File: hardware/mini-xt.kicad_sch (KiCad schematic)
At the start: 0 parts

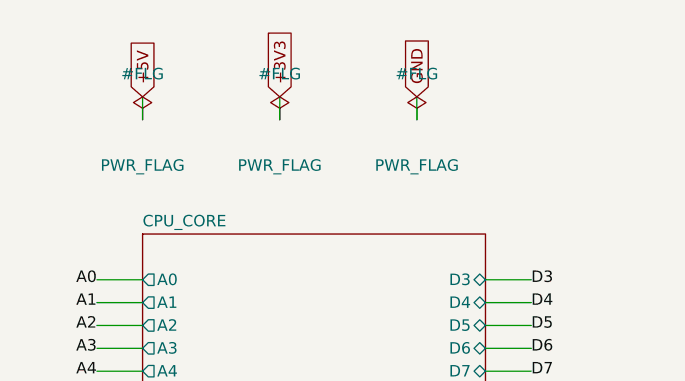
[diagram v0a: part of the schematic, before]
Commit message: ERC power cleanup: single flag owner, flags on series-fed rails
Full-build ERC is now just the 6 expected IRQ9-13/15 label_dangling.

- Root's duplicate PWR_FLAGs removed from build.py: power.py #FLG1-3
  own +5V/+3V3/GND; the pair made flag-vs-flag pin_to_pin errors.
- PWR_FLAGs added on the local rails ERC can't see through a series
  part: VBUS_MCU / VBUS_VID (Schottky diode-OR), VBUS_KBD / HDMI_5V
  (polyfuse), CH224_VDD (1k per WCH ref), AVDD_PGUS / AGND_PGUS
  (ferrite beads).

Net membership verified unchanged: 821 nets, node-identical to HEAD.

Co-Authored-By: Claude Fable 5 <noreply@anthropic.com>
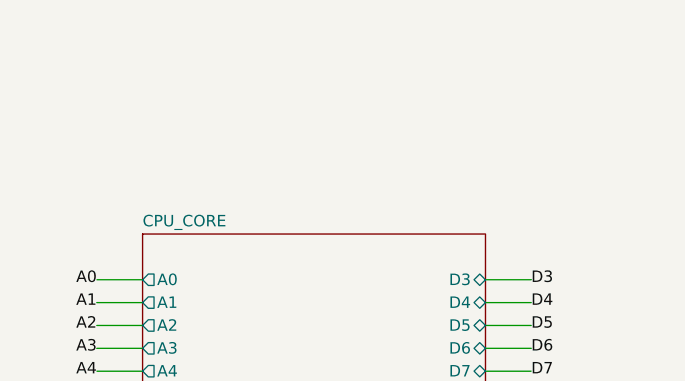
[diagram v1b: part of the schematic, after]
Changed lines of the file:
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@@
-		)
-	)
-	(wire
-		(pts
-			(xy 25.4 12.7)
-			(xy 25.4 10.16)
-		)
-		(stroke
-			(width 0)
-			(type default)
-		)
-	)
-	(global_label "+5V"
-		(shape input)
-		(at 25.4 10.16 90)
-		(effects
-			(font
-				(size 1.27 1.27)
-			)
-		)
-	)
-	(wire
-		(pts
-			(xy 40.64 12.7)
-			(xy 40.64 10.16)
-		)
-		(stroke
-			(width 0)
-			(type default)
-		)
-	)
-	(global_label "+3V3"
-		(shape input)
-		(at 40.64 10.16 90)
-		(effects
-			(font
-				(size 1.27 1.27)
-			)
-		)
-	)
-	(wire
-		(pts
-			(xy 55.88 12.7)
-			(xy 55.88 10.16)
-		)
-		(stroke
-			(width 0)
-			(type default)
-		)
-	)
-	(global_label "GND"
-		(shape input)
-		(at 55.88 10.16 90)
-		(effects
-			(font
-				(size 1.27 1.27)
-			)
-		)
-	)
-	(symbol
-		(lib_id "power:PWR_FLAG")
-		(at 25.4 12.7 0)
-		(unit 1)
-		(exclude_from_sim no)
-		(in_bom yes)
-		(on_board yes)
-		(dnp no)
-		(fields_autoplaced yes)
-		(property "Reference" "#FLG"
-			(at 25.4 7.62 0)
-			(effects
-				(font
-					(size 1.27 1.27)
-				)
-			)
-		)
-		(property "Value" "PWR_FLAG"
-			(at 25.4 17.78 0)
-			(effects
-				(font
-					(size 1.27 1.27)
-				)
-			)
-		)
-		(property "Footprint" ""
-			(at 25.4 12.7 0)
-			(effects
-				(font
-					(size 1.27 1.27)
-				)
-				(hide yes)
-			)
-		)
-		(pin "1"
-		)
-		(instances
-			(project "mini-xt"
-				(path "/26736c46-8b40-5460-874f-03596d17270c"
-					(reference "#FLG")
-					(unit 1)
-				)
-			)
-		)
-	)
-	(symbol
-		(lib_id "power:PWR_FLAG")
-		(at 40.64 12.7 0)
-		(unit 1)
-		(exclude_from_sim no)
-		(in_bom yes)
-		(on_board yes)
-		(dnp no)
-		(fields_autoplaced yes)
-		(property "Reference" "#FLG"
-			(at 40.64 7.62 0)
-			(effects
-				(font
-					(size 1.27 1.27)
-				)
-			)
-		)
-		(property "Value" "PWR_FLAG"
-			(at 40.64 17.78 0)
-			(effects
-				(font
-					(size 1.27 1.27)
-				)
-			)
-		)
-		(property "Footprint" ""
-			(at 40.64 12.7 0)
-			(effects
-				(font
-					(size 1.27 1.27)
-				)
-				(hide yes)
-			)
-		)
-		(pin "1"
-		)
-		(instances
-			(project "mini-xt"
-				(path "/26736c46-8b40-5460-874f-03596d17270c"
-					(reference "#FLG")
-					(unit 1)
-				)
-			)
-		)
-	)
-	(symbol
-		(lib_id "power:PWR_FLAG")
-		(at 55.88 12.7 0)
-		(unit 1)
-		(exclude_from_sim no)
-		(in_bom yes)
-		(on_board yes)
-		(dnp no)
-		(fields_autoplaced yes)
-		(property "Reference" "#FLG"
-			(at 55.88 7.62 0)
-			(effects
-				(font
-					(size 1.27 1.27)
-				)
-			)
-		)
-		(property "Value" "PWR_FLAG"
-			(at 55.88 17.78 0)
-			(effects
-				(font
-					(size 1.27 1.27)
-				)
-			)
-		)
-		(property "Footprint" ""
-			(at 55.88 12.7 0)
-			(effects
-				(font
-					(size 1.27 1.27)
-				)
-				(hide yes)
-			)
-		)
-		(pin "1"
-		)
-		(instances
-			(project "mini-xt"
-				(path "/26736c46-8b40-5460-874f-03596d17270c"
-					(reference "#FLG")
-					(unit 1)
-				)
-			)
 		)
 	)

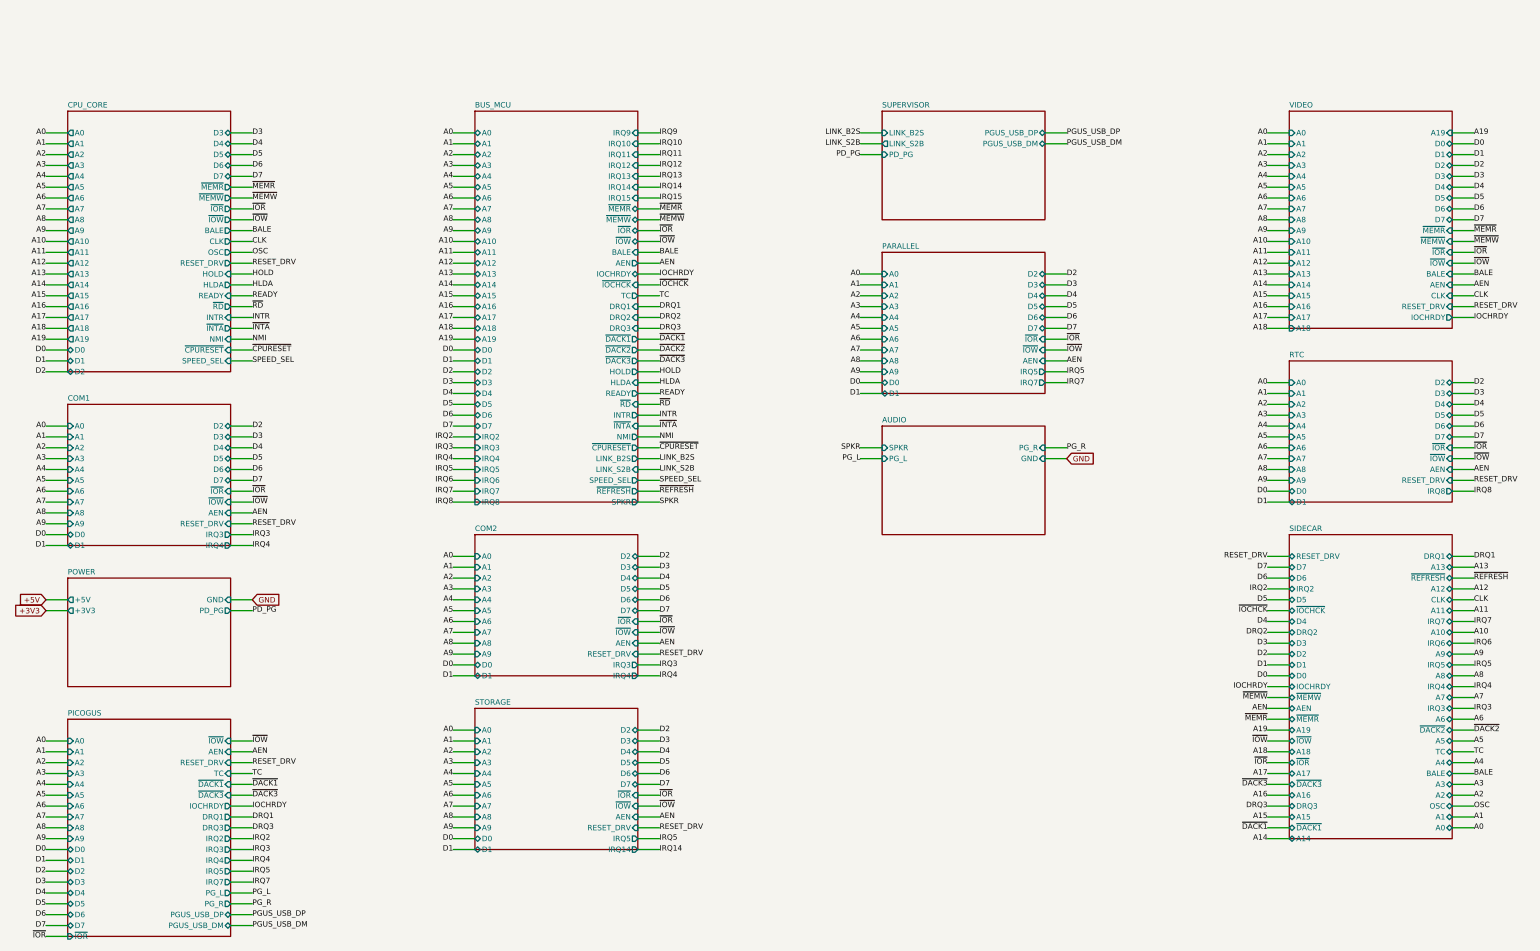
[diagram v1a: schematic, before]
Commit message: IRQ rework: single-'165 collector, hardwired COM/LPT IRQs
- IRQ collector shrunk to one 74HCT165: D0-D6 = IRQ2-8, D7 = IRQ14
  (replacing the source-less IRQ9). U19 + pull-downs R19-R24 + C18
  deleted; IRQ9-13/15 dropped everywhere (nothing on the board or the
  8-bit header can drive them). Firmware shifts 8 bits, Q7-first.
- COM/LPT IRQ straps deleted, hardwired to the PC conventions:
  COM1=IRQ4, COM2=IRQ3 (COM_IRQ per-instance netmap remap -- first use
  of the INSTANCES netmap), LPT=IRQ7 (U13 '125 drives the net
  directly). The enable jumpers (COM JP3, LPT JP2) free an IRQ by
  disabling the port; the tri-state drivers go silent with it.
- Storage JP3 (IRQ14/IRQ5) kept: both positions are real conventions
  (AT vs XT), not conflict avoidance. Its IRQ5 warning now points at
  the PicoGUS jumper block, the only remaining IRQ5 contention.
- Design doc: fix stale claim that IRQ8 rides a reclaimed header pin
  (that pin is a ground return; IRQ8 is motherboard-internal).

Full-build ERC: 0 violations.

Co-Authored-By: Claude Fable 5 <noreply@anthropic.com>
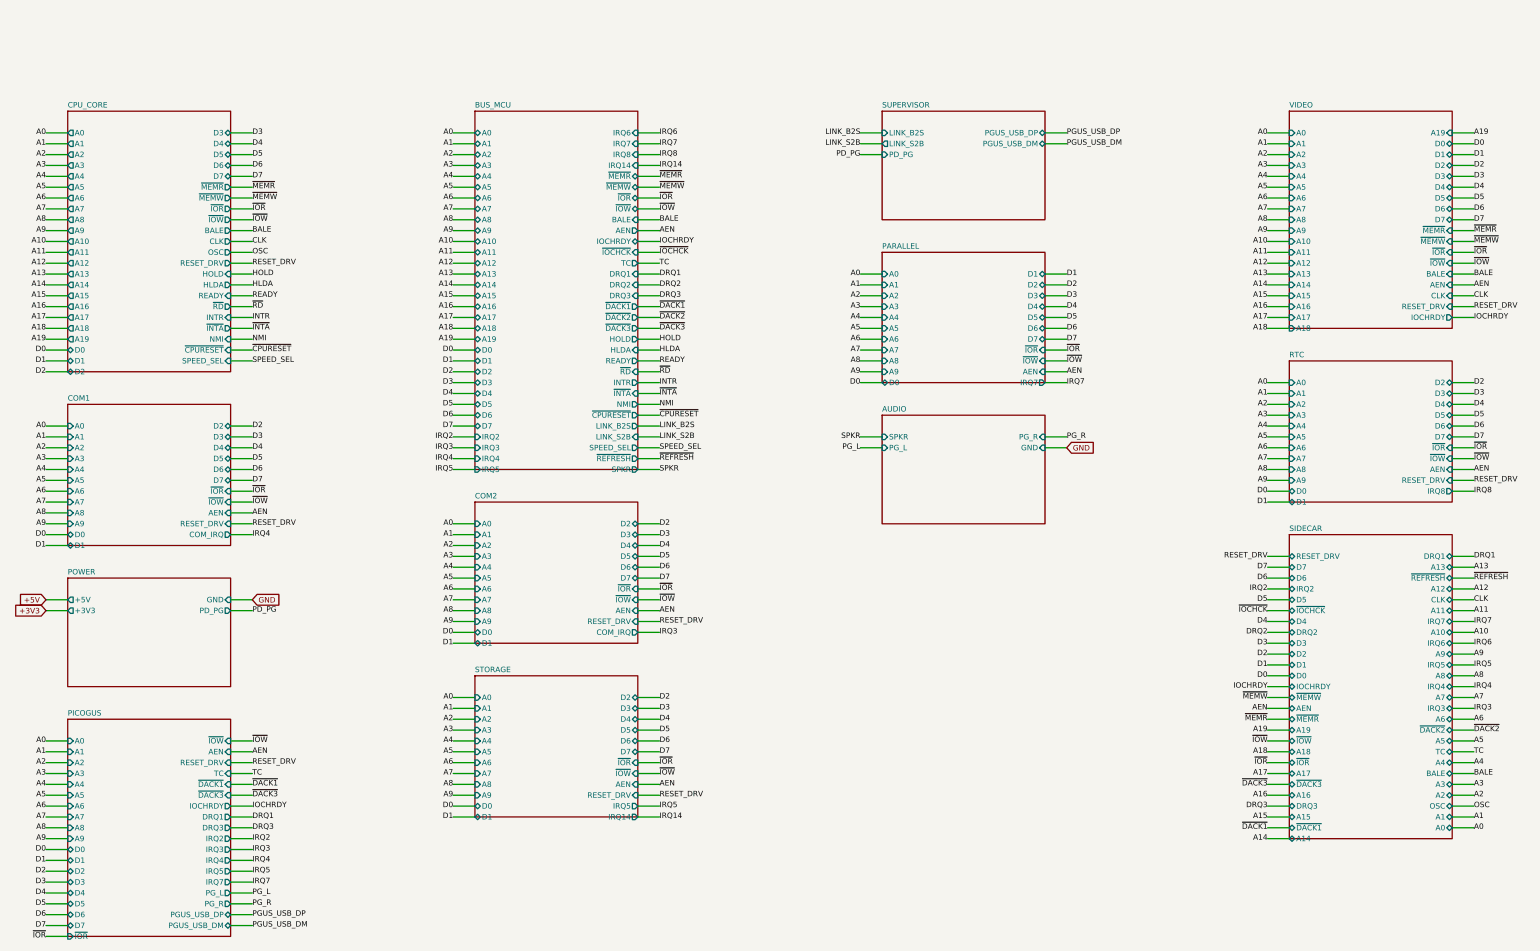
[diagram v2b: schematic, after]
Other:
- sheet BUS_MCU ports: added none; removed IRQ10, IRQ11, IRQ12, IRQ13, IRQ15, IRQ9
- sheet COM1 ports: added COM_IRQ; removed IRQ3, IRQ4
- sheet COM2 ports: added COM_IRQ; removed IRQ3, IRQ4
- sheet PARALLEL ports: added none; removed IRQ5

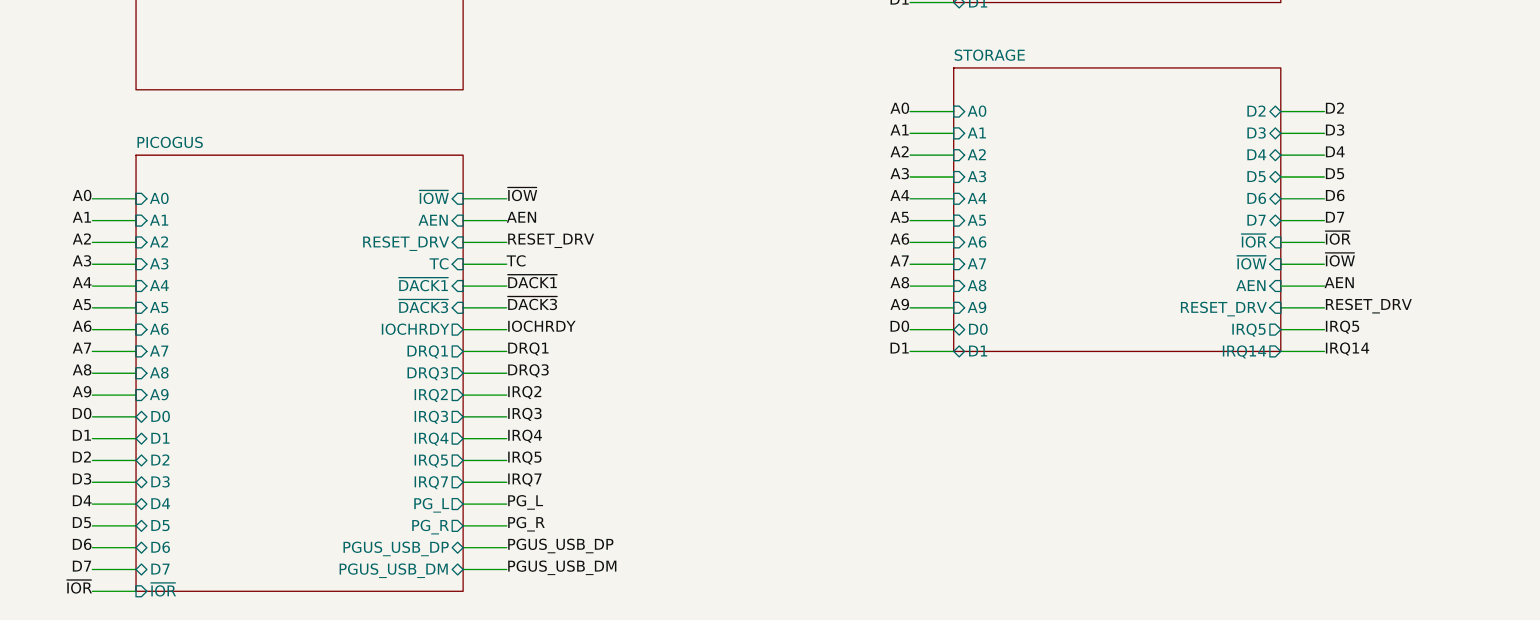
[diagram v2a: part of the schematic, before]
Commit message: Hardwire storage IRQ14 and PicoGUS IRQ5; drop their IRQ jumpers
- Storage JP3 deleted: INTRQ -> '125 -> IRQ14 directly (the soft PIC
  is AT-style anyway). Poll vs interrupt is an XTIDE UB per-controller
  config choice, safe with the line wired either way -- the tri-state
  driver is silent unless the drive asserts INTRQ. ~{IRQ5_OE} renamed
  ~{IRQ_OE} to match.
- PicoGUS IRQ jumper row deleted: the shifter output drives IRQ5
  directly -- the free line and now its sole driver; every personality
  works on IRQ5 and pgusinit sets the firmware to match, so the 5-row
  jumper bought nothing. J1 shrinks 2x9 -> 2x4 (DMA pairs only, ch1 is
  the only MCU-serviced channel); parts.py header entry follows.
- IRQ5 contention is now zero: the sidecar header is the only other
  possible driver.

Full-build ERC: 0 violations; cards build clean.

Co-Authored-By: Claude Fable 5 <noreply@anthropic.com>
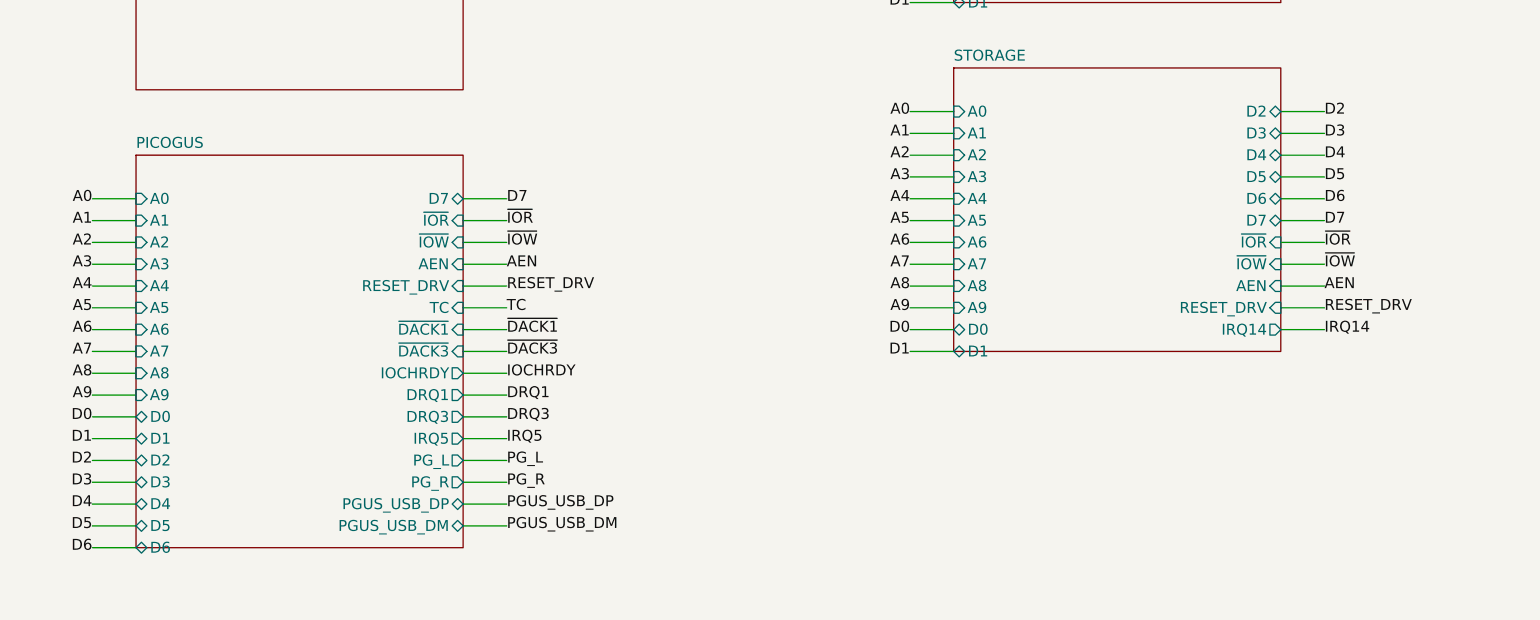
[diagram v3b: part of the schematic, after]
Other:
- sheet PICOGUS ports: added none; removed IRQ2, IRQ3, IRQ4, IRQ7
- sheet STORAGE ports: added none; removed IRQ5
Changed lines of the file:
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@@
 			)
 		)
-		(pin "IRQ5" output
-			(at 158.75 187.96 0)
-			(effects
-				(font
-					(size 1.27 1.27)
-				)
-				(justify left)
-			)
-		)
 		(pin "IRQ14" output
-			(at 158.75 190.5 0)
+			(at 158.75 187.96 0)
 			(effects
 				(font
@@
 	(sheet
 		(at 25.4 167.64)
-		(size 38.1 50.8)
+		(size 38.1 45.72)
 		(exclude_from_sim no)
 		(in_bom yes)
@@
 		)
 		(property "Sheetfile" "sheets/picogus.kicad_sch"
-			(at 25.4 219.14 0)
+			(at 25.4 214.06 0)
 			(effects
 				(font
@@
 		)
 		(pin "D7" bidirectional
-			(at 25.4 215.9 180)
-			(effects
-				(font
-					(size 1.27 1.27)
-				)
-				(justify right)
-			)
-		)
-		(pin "~{IOR}" input
-			(at 25.4 218.44 180)
-			(effects
-				(font
-					(size 1.27 1.27)
-				)
-				(justify right)
-			)
-		)
-		(pin "~{IOW}" input
 			(at 63.5 172.72 0)
 			(effects
@@
 			)
 		)
-		(pin "AEN" input
+		(pin "~{IOR}" input
 			(at 63.5 175.26 0)
 			(effects
@@
 			)
 		)
-		(pin "RESET_DRV" input
+		(pin "~{IOW}" input
 			(at 63.5 177.8 0)
 			(effects
@@
 			)
 		)
-		(pin "TC" input
+		(pin "AEN" input
 			(at 63.5 180.34 0)
 			(effects
@@
 			)
 		)
-		(pin "~{DACK1}" input
+		(pin "RESET_DRV" input
 			(at 63.5 182.88 0)
 			(effects
@@
 			)
 		)
-		(pin "~{DACK3}" input
+		(pin "TC" input
 			(at 63.5 185.42 0)
 			(effects
@@
 			)
 		)
-		(pin "IOCHRDY" output
+		(pin "~{DACK1}" input
 			(at 63.5 187.96 0)
 			(effects
@@
 			)
 		)
-		(pin "DRQ1" output
+		(pin "~{DACK3}" input
 			(at 63.5 190.5 0)
 			(effects
@@
 			)
 		)
-		(pin "DRQ3" output
+		(pin "IOCHRDY" output
 			(at 63.5 193.04 0)
 			(effects
@@
 			)
 		)
-		(pin "IRQ2" output
+		(pin "DRQ1" output
 			(at 63.5 195.58 0)
 			(effects
@@
 			)
 		)
-		(pin "IRQ3" output
+		(pin "DRQ3" output
 			(at 63.5 198.12 0)
 			(effects
@@
 			)
 		)
-		(pin "IRQ4" output
-			(at 63.5 200.66 0)
-			(effects
-				(font
-					(size 1.27 1.27)
-				)
-				(justify left)
-			)
-		)
 		(pin "IRQ5" output
-			(at 63.5 203.2 0)
-			(effects
-				(font
-					(size 1.27 1.27)
-				)
-				(justify left)
-			)
-		)
-		(pin "IRQ7" output
-			(at 63.5 205.74 0)
+			(at 63.5 200.66 0)
 			(effects
 				(font
@@
 		)
 		(pin "PG_L" output
-			(at 63.5 208.28 0)
+			(at 63.5 203.2 0)
 			(effects
 				(font
@@
 		)
 		(pin "PG_R" output
-			(at 63.5 210.82 0)
+			(at 63.5 205.74 0)
 			(effects
 				(font
@@
 		)
 		(pin "PGUS_USB_DP" bidirectional
-			(at 63.5 213.36 0)
+			(at 63.5 208.28 0)
 			(effects
 				(font
@@
 		)
 		(pin "PGUS_USB_DM" bidirectional
-			(at 63.5 215.9 0)
+			(at 63.5 210.82 0)
 			(effects
 				(font
@@
 		)
 	)
-	(label "IRQ5"
-		(at 163.83 187.96 0)
-		(effects
-			(font
-				(size 1.27 1.27)
-			)
-			(justify left)
-		)
-	)
-	(wire
-		(pts
-			(xy 158.75 190.5)
-			(xy 163.83 190.5)
-		)
-		(stroke
-			(width 0)
-			(type default)
-		)
-	)
 	(label "IRQ14"
-		(at 163.83 190.5 0)
+		(at 163.83 187.96 0)
 		(effects
 			(font
@@
 	(wire
 		(pts
-			(xy 25.4 215.9)
-			(xy 20.32 215.9)
-		)
-		(stroke
-			(width 0)
-			(type default)
-		)
-	)
-	(label "D7"
-		(at 20.32 215.9 180)
-		(effects
-			(font
-				(size 1.27 1.27)
-			)
-			(justify right)
-		)
-	)
-	(wire
-		(pts
-			(xy 25.4 218.44)
-			(xy 20.32 218.44)
-		)
-		(stroke
-			(width 0)
-			(type default)
-		)
-	)
-	(label "~{IOR}"
-		(at 20.32 218.44 180)
-		(effects
-			(font
-				(size 1.27 1.27)
-			)
-			(justify right)
-		)
-	)
-	(wire
-		(pts
 			(xy 63.5 172.72)
 			(xy 68.58 172.72)
@@
 		)
 	)
-	(label "~{IOW}"
+	(label "D7"
 		(at 68.58 172.72 0)
 		(effects
@@
 		)
 	)
-	(label "AEN"
+	(label "~{IOR}"
 		(at 68.58 175.26 0)
 		(effects
@@
 		)
 	)
-	(label "RESET_DRV"
+	(label "~{IOW}"
 		(at 68.58 177.8 0)
 		(effects
@@
 		)
 	)
-	(label "TC"
+	(label "AEN"
 		(at 68.58 180.34 0)
 		(effects
@@
 		)
 	)
-	(label "~{DACK1}"
+	(label "RESET_DRV"
 		(at 68.58 182.88 0)
 		(effects
@@
 		)
 	)
-	(label "~{DACK3}"
+	(label "TC"
 		(at 68.58 185.42 0)
 		(effects
@@
 		)
 	)
-	(label "IOCHRDY"
+	(label "~{DACK1}"
 		(at 68.58 187.96 0)
 		(effects
@@
 		)
 	)
-	(label "DRQ1"
+	(label "~{DACK3}"
 		(at 68.58 190.5 0)
 		(effects
@@
 		)
 	)
-	(label "DRQ3"
+	(label "IOCHRDY"
 		(at 68.58 193.04 0)
 		(effects
@@
 		)
 	)
-	(label "IRQ2"
+	(label "DRQ1"
 		(at 68.58 195.58 0)
 		(effects
@@
 		)
 	)
-	(label "IRQ3"
+	(label "DRQ3"
 		(at 68.58 198.12 0)
 		(effects
@@
 		)
 	)
-	(label "IRQ4"
+	(label "IRQ5"
 		(at 68.58 200.66 0)
 		(effects
@@
 		)
 	)
-	(label "IRQ5"
+	(label "PG_L"
 		(at 68.58 203.2 0)
 		(effects
@@
 		)
 	)
-	(label "IRQ7"
+	(label "PG_R"
 		(at 68.58 205.74 0)
 		(effects
@@
 		)
 	)
-	(label "PG_L"
+	(label "PGUS_USB_DP"
 		(at 68.58 208.28 0)
 		(effects
@@
 		)
 	)
-	(label "PG_R"
-		(at 68.58 210.82 0)
-		(effects
-			(font
-				(size 1.27 1.27)
-			)
-			(justify left)
-		)
-	)
-	(wire
-		(pts
-			(xy 63.5 213.36)
-			(xy 68.58 213.36)
-		)
-		(stroke
-			(width 0)
-			(type default)
-		)
-	)
-	(label "PGUS_USB_DP"
-		(at 68.58 213.36 0)
-		(effects
-			(font
-				(size 1.27 1.27)
-			)
-			(justify left)
-		)
-	)
-	(wire
-		(pts
-			(xy 63.5 215.9)
-			(xy 68.58 215.9)
-		)
-		(stroke
-			(width 0)
-			(type default)
-		)
-	)
 	(label "PGUS_USB_DM"
-		(at 68.58 215.9 0)
+		(at 68.58 210.82 0)
 		(effects
 			(font
